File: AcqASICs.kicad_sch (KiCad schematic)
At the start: 54 parts, among them U21 1821-3936, U22 1821-3936

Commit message: Add component values, some more nets
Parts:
- C521, C528, C529, C530, C531, C532, C539, C540, C541, C542, C543, C544: value ? -> 3.3nF
- C523, C524, C525, C526, C527, C534, C535, C536, C537, C538: value ? -> 360pF
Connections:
- net U21_BI18 is gone; now on net U21_BI8: U21.R26 (SIOR)
- net IDB12: now reaches U22.D18 (IDB12)
- net IDB12: now also U21.D18 (IDB12)
- net IDB6: now reaches U22.D19 (IDB6)
- net IDB6: now also U21.D19 (IDB6)
- net IDB0: now reaches U22.D20 (IDB0)
- net IDB0: now also U21.D20 (IDB0)
- net IDB4: now reaches U22.E19 (IDB4)
- net IDB4: now also U21.E19 (IDB4)
- net U39_15: now reaches U22.AA2 (V8.15)
- net U52_9: now reaches U22.AA4 (V5.9)
- net U52_7: now reaches U22.AA5 (V5.7)
- net U52_10: now reaches U22.AB3 (V5.10)
- net U52_4: now reaches U22.AB4 (V5.4)
- net U52_6: now reaches U22.AB5 (V5.6)
- net U52_5: now reaches U22.AC2 (V5.5)
- net U52_13: now reaches U22.AC3 (V5.13)
- net U52_1: now reaches U22.AC4 (V5.1)
- net U52_11: now reaches U22.AC5 (V5.11)
- net U52_12: now reaches U22.AD1 (V5.12)
- net U52_2: now reaches U22.AD2 (V5.2)
- net U52_0: now reaches U22.AD3 (V5.0)
- net U52_3: now reaches U22.AD5 (V5.3)
- net U42_11: now reaches U22.AE10 (V7.11)
- net U42_6: now reaches U22.AE11 (V7.6)
- net U42_8: now reaches U22.AE12 (V7.8)
- net U52_15: now reaches U22.AE2 (V5.15)
- net U52_14: now reaches U22.AE4 (V5.14)
- net U32_14: now reaches U22.AE5 (V6.14)
- net U32_6: now reaches U22.AE6 (V6.6)
- net U32_8: now reaches U22.AE7 (V6.8)
- net U42_14: now reaches U22.AE8 (V7.14)
- net U42_3: now reaches U22.AE9 (V7.3)
- net U42_5: now reaches U22.AF10 (V7.5)
- net U42_9: now reaches U22.AF11 (V7.9)
- net U32_0: now reaches U22.AF2 (V6.0)
- net U32_1: now reaches U22.AF3 (V6.1)
- net U32_12: now reaches U22.AF4 (V6.12)
- net U32_4: now reaches U22.AF5 (V6.4)
- net U32_9: now reaches U22.AF6 (V6.9)
- net U42_0: now reaches U22.AF7 (V7.0)
- net U42_2: now reaches U22.AF8 (V7.2)
- net U42_12: now reaches U22.AF9 (V7.12)
- net U42_10: now reaches U22.AG10 (V7.10)
- net U42_7: now reaches U22.AG11 (V7.7)
- net U32_15: now reaches U22.AG2 (V6.15)
- net U32_2: now reaches U22.AG3 (V6.2)
- net U32_10: now reaches U22.AG4 (V6.10)
- net U32_11: now reaches U22.AG5 (V6.11)
- net U32_7: now reaches U22.AG6 (V6.7)
- net U42_15: now reaches U22.AG7 (V7.15)
- net U42_13: now reaches U22.AG8 (V7.13)
- net U42_4: now reaches U22.AG9 (V7.4)
- net U32_3: now reaches U22.AH2 (V6.3)
- net U32_5: now reaches U22.AH3 (V6.5)
- net U50_4: now reaches U22.B3 (V1.4)
- net U58_11: now reaches U22.C10 (V0.11)
- net U58_6: now reaches U22.C11 (V0.6)
- net U58_8: now reaches U22.C12 (V0.8)
- net U50_11: now reaches U22.C4 (V1.11)
- net U50_12: now reaches U22.C5 (V1.12)
- net U50_6: now reaches U22.C6 (V1.6)
- net U50_8: now reaches U22.C7 (V1.8)
- net U58_14: now reaches U22.C8 (V0.14)
- net U58_3: now reaches U22.C9 (V0.3)
- net U58_4: now reaches U22.D10 (V0.4)
- net U58_10: now reaches U22.D11 (V0.10)
- net U58_7: now reaches U22.D12 (V0.7)
- net U50_15: now reaches U22.D14 (V1.15)
- net U50_0: now reaches U22.D2 (V1.0)
- net U50_1: now reaches U22.D3 (V1.1)
- net U50_3: now reaches U22.D4 (V1.3)
- net U50_13: now reaches U22.D5 (V1.13)
- net U50_10: now reaches U22.D6 (V1.10)
- net U50_7: now reaches U22.D7 (V1.7)
- net U58_1: now reaches U22.D8 (V0.1)
- net U58_13: now reaches U22.D9 (V0.13)
- net U58_12: now reaches U22.E10 (V0.12)
- net U58_5: now reaches U22.E11 (V0.5)
- net U58_9: now reaches U22.E12 (V0.9)
- net U50_2: now reaches U22.E13 (V1.2)
- net U30_15: now reaches U22.E2 (V2.15)
- net U30_1: now reaches U22.E3 (V2.1)
- net U30_0: now reaches U22.E4 (V2.0)
- net U50_14: now reaches U22.E5 (V1.14)
- net U50_5: now reaches U22.E6 (V1.5)
- net U50_9: now reaches U22.E7 (V1.9)
- net U58_15: now reaches U22.E8 (V0.15)
- net U58_2: now reaches U22.E9 (V0.2)
- net U30_11: now reaches U22.F1 (V2.11)
- net U30_13: now reaches U22.F2 (V2.13)
- net U30_3: now reaches U22.F3 (V2.3)
- net U30_2: now reaches U22.F4 (V2.2)
- net U30_14: now reaches U22.F5 (V2.14)
- net U30_10: now reaches U22.G2 (V2.10)
- net U30_5: now reaches U22.G3 (V2.5)
- net U30_4: now reaches U22.G4 (V2.4)
- net U30_12: now reaches U22.G5 (V2.12)
- net U39_0: now reaches U22.H2 (V8.0)
- net U30_7: now reaches U22.H3 (V2.7)
- net U30_6: now reaches U22.H4 (V2.6)
- net U30_9: now reaches U22.H5 (V2.9)
- net U39_1: now reaches U22.J2 (V8.1)
- net U40_15: now reaches U22.J3 (V3.15)
- net U30_8: now reaches U22.J4 (V2.8)
- net U40_0: now reaches U22.J5 (V3.0)
- net U39_2: now reaches U22.K2 (V8.2)
- net U40_2: now reaches U22.K3 (V3.2)
- net U40_1: now reaches U22.K4 (V3.1)
- net U40_14: now reaches U22.K5 (V3.14)
- net U39_3: now reaches U22.L2 (V8.3)
- net U40_12: now reaches U22.L3 (V3.12)
- net U40_13: now reaches U22.L4 (V3.13)
- net U40_3: now reaches U22.L5 (V3.3)
- net U39_4: now reaches U22.M2 (V8.4)
- net U40_5: now reaches U22.M3 (V3.5)
- net U40_4: now reaches U22.M4 (V3.4)
- net U40_11: now reaches U22.M5 (V3.11)
- net U39_6: now reaches U22.N1 (V8.6)
- net U39_5: now reaches U22.N2 (V8.5)
- net U40_9: now reaches U22.N3 (V3.9)
- net U40_6: now reaches U22.N4 (V3.6)
- net U40_10: now reaches U22.N5 (V3.10)
- net U39_7: now reaches U22.P2 (V8.7)
- net U40_8: now reaches U22.P3 (V3.8)
- net U40_7: now reaches U22.P5 (V3.7)
- net U39_8: now reaches U22.R2 (V8.8)
- net U60_8: now reaches U22.R4 (V4.8)
- net U60_7: now reaches U22.R5 (V4.7)
- net U39_9: now reaches U22.T2 (V8.9)
- net U60_9: now reaches U22.T3 (V4.9)
- net U60_10: now reaches U22.T4 (V4.10)
- net U60_6: now reaches U22.T5 (V4.6)
- net U39_11: now reaches U22.U1 (V8.11)
- net U39_10: now reaches U22.U2 (V8.10)
- net U60_5: now reaches U22.U3 (V4.5)
- net U60_4: now reaches U22.U4 (V4.4)
- net U60_11: now reaches U22.U5 (V4.11)
- net U39_12: now reaches U22.V2 (V8.12)
- net U60_12: now reaches U22.V3 (V4.12)
- net U60_13: now reaches U22.V4 (V4.13)
- net U60_3: now reaches U22.V5 (V4.3)
- net U39_13: now reaches U22.W2 (V8.13)
- net U60_2: now reaches U22.W3 (V4.2)
- net U60_1: now reaches U22.W4 (V4.1)
- net U60_14: now reaches U22.W5 (V4.14)
- net U39_14: now reaches U22.Y2 (V8.14)
- net U60_15: now reaches U22.Y3 (V4.15)
- net U52_8: now reaches U22.Y4 (V5.8)
- net U60_0: now reaches U22.Y5 (V4.0)
- net U29_15: now reaches U21.AA2 (V8.15)
- net U48_9: now reaches U21.AA4 (V5.9)
- net U48_7: now reaches U21.AA5 (V5.7)
- net U48_10: now reaches U21.AB3 (V5.10)
- net U48_4: now reaches U21.AB4 (V5.4)
- net U48_6: now reaches U21.AB5 (V5.6)
- net U48_5: now reaches U21.AC2 (V5.5)
- net U48_13: now reaches U21.AC3 (V5.13)
- net U48_1: now reaches U21.AC4 (V5.1)
- net U48_11: now reaches U21.AC5 (V5.11)
- net U48_12: now reaches U21.AD1 (V5.12)
- net U48_2: now reaches U21.AD2 (V5.2)
- net U48_0: now reaches U21.AD3 (V5.0)
- net U48_3: now reaches U21.AD5 (V5.3)
- net U37_11: now reaches U21.AE10 (V7.11)
- net U37_6: now reaches U21.AE11 (V7.6)
- net U37_8: now reaches U21.AE12 (V7.8)
- net U48_15: now reaches U21.AE2 (V5.15)
- net U48_14: now reaches U21.AE4 (V5.14)
- net U27_14: now reaches U21.AE5 (V6.14)
- net U27_6: now reaches U21.AE6 (V6.6)
- net U27_8: now reaches U21.AE7 (V6.8)
- net U37_14: now reaches U21.AE8 (V7.14)
- net U37_3: now reaches U21.AE9 (V7.3)
- net U37_5: now reaches U21.AF10 (V7.5)
- net U37_9: now reaches U21.AF11 (V7.9)
- net U27_0: now reaches U21.AF2 (V6.0)
- net U27_1: now reaches U21.AF3 (V6.1)
- net U27_12: now reaches U21.AF4 (V6.12)
- net U27_4: now reaches U21.AF5 (V6.4)
- net U27_9: now reaches U21.AF6 (V6.9)
- net U37_0: now reaches U21.AF7 (V7.0)
- net U37_2: now reaches U21.AF8 (V7.2)
- net U37_12: now reaches U21.AF9 (V7.12)
- net U37_10: now reaches U21.AG10 (V7.10)
- net U37_7: now reaches U21.AG11 (V7.7)
- net U27_15: now reaches U21.AG2 (V6.15)
- net U27_2: now reaches U21.AG3 (V6.2)
- net U27_10: now reaches U21.AG4 (V6.10)
- net U27_11: now reaches U21.AG5 (V6.11)
- net U27_7: now reaches U21.AG6 (V6.7)
- net U37_15: now reaches U21.AG7 (V7.15)
- net U37_13: now reaches U21.AG8 (V7.13)
- net U37_4: now reaches U21.AG9 (V7.4)
- net U27_3: now reaches U21.AH2 (V6.3)
- net U27_5: now reaches U21.AH3 (V6.5)
- net U46_4: now reaches U21.B3 (V1.4)
- net U54_11: now reaches U21.C10 (V0.11)
- net U54_6: now reaches U21.C11 (V0.6)
- net U54_8: now reaches U21.C12 (V0.8)
- net U46_11: now reaches U21.C4 (V1.11)
- net U46_12: now reaches U21.C5 (V1.12)
- net U46_6: now reaches U21.C6 (V1.6)
- net U46_8: now reaches U21.C7 (V1.8)
- net U54_14: now reaches U21.C8 (V0.14)
- net U54_3: now reaches U21.C9 (V0.3)
- net U54_4: now reaches U21.D10 (V0.4)
- net U54_10: now reaches U21.D11 (V0.10)
- net U54_7: now reaches U21.D12 (V0.7)
- net U46_15: now reaches U21.D14 (V1.15)
- net U46_0: now reaches U21.D2 (V1.0)
- net U46_1: now reaches U21.D3 (V1.1)
- net U46_3: now reaches U21.D4 (V1.3)
- net U46_13: now reaches U21.D5 (V1.13)
- net U46_10: now reaches U21.D6 (V1.10)
- net U46_7: now reaches U21.D7 (V1.7)
- net U54_1: now reaches U21.D8 (V0.1)
- net U54_13: now reaches U21.D9 (V0.13)
- net U54_12: now reaches U21.E10 (V0.12)
- net U54_5: now reaches U21.E11 (V0.5)
- net U54_9: now reaches U21.E12 (V0.9)
- net U46_2: now reaches U21.E13 (V1.2)
- net U25_15: now reaches U21.E2 (V2.15)
- net U25_1: now reaches U21.E3 (V2.1)
- net U25_0: now reaches U21.E4 (V2.0)
- net U46_14: now reaches U21.E5 (V1.14)
- net U46_5: now reaches U21.E6 (V1.5)
- net U46_9: now reaches U21.E7 (V1.9)
- net U54_15: now reaches U21.E8 (V0.15)
- net U54_2: now reaches U21.E9 (V0.2)
- net U25_11: now reaches U21.F1 (V2.11)
- net U25_13: now reaches U21.F2 (V2.13)
- net U25_3: now reaches U21.F3 (V2.3)
- net U25_2: now reaches U21.F4 (V2.2)
- net U25_14: now reaches U21.F5 (V2.14)
- net U25_10: now reaches U21.G2 (V2.10)
- net U25_5: now reaches U21.G3 (V2.5)
- net U25_4: now reaches U21.G4 (V2.4)
- net U25_12: now reaches U21.G5 (V2.12)
- net U29_0: now reaches U21.H2 (V8.0)
- net U25_7: now reaches U21.H3 (V2.7)
- net U25_6: now reaches U21.H4 (V2.6)
- net U25_9: now reaches U21.H5 (V2.9)
- net U29_1: now reaches U21.J2 (V8.1)
- net U35_15: now reaches U21.J3 (V3.15)
- net U25_8: now reaches U21.J4 (V2.8)
- net U35_0: now reaches U21.J5 (V3.0)
- net U29_2: now reaches U21.K2 (V8.2)
- net U35_2: now reaches U21.K3 (V3.2)
- net U35_1: now reaches U21.K4 (V3.1)
- net U35_14: now reaches U21.K5 (V3.14)
- net U29_3: now reaches U21.L2 (V8.3)
- net U35_12: now reaches U21.L3 (V3.12)
- net U35_13: now reaches U21.L4 (V3.13)
- net U35_3: now reaches U21.L5 (V3.3)
- net U29_4: now reaches U21.M2 (V8.4)
- net U35_5: now reaches U21.M3 (V3.5)
- net U35_4: now reaches U21.M4 (V3.4)
- net U35_11: now reaches U21.M5 (V3.11)
- net U29_6: now reaches U21.N1 (V8.6)
- net U29_5: now reaches U21.N2 (V8.5)
- net U35_9: now reaches U21.N3 (V3.9)
- net U35_6: now reaches U21.N4 (V3.6)
- net U35_10: now reaches U21.N5 (V3.10)
- net U29_7: now reaches U21.P2 (V8.7)
- net U35_8: now reaches U21.P3 (V3.8)
- net U35_7: now reaches U21.P5 (V3.7)
- net U29_8: now reaches U21.R2 (V8.8)
- net U56_8: now reaches U21.R4 (V4.8)
- net U56_7: now reaches U21.R5 (V4.7)
- net U29_9: now reaches U21.T2 (V8.9)
- net U56_9: now reaches U21.T3 (V4.9)
- net U56_10: now reaches U21.T4 (V4.10)
- net U56_6: now reaches U21.T5 (V4.6)
- net U29_11: now reaches U21.U1 (V8.11)
- net U29_10: now reaches U21.U2 (V8.10)
- net U56_5: now reaches U21.U3 (V4.5)
- net U56_4: now reaches U21.U4 (V4.4)
- net U56_11: now reaches U21.U5 (V4.11)
- net U29_12: now reaches U21.V2 (V8.12)
- net U56_12: now reaches U21.V3 (V4.12)
- net U56_13: now reaches U21.V4 (V4.13)
- net U56_3: now reaches U21.V5 (V4.3)
- net U29_13: now reaches U21.W2 (V8.13)
- net U56_2: now reaches U21.W3 (V4.2)
- net U56_1: now reaches U21.W4 (V4.1)
- net U56_14: now reaches U21.W5 (V4.14)
- net U29_14: now reaches U21.Y2 (V8.14)
- net U56_15: now reaches U21.Y3 (V4.15)
- net U48_8: now reaches U21.Y4 (V5.8)
- net U56_0: now reaches U21.Y5 (V4.0)
- net ACQ1_CAP1 renamed POD2A_VREF
- net POD2A_VREF: now also U21.Y26 (VREF3); no longer U21.Y26 (CAP4)
- net ACQ1_CAP2 renamed POD1A_VREF
- net POD1A_VREF: now also U21.Y25 (VREF1); no longer U21.Y25 (CAP3)
- net ACQ1_CAP3 renamed POD1B_VREF
- net POD1B_VREF: now also U21.L25 (VREF2); no longer U21.L25 (CAP2)
- net ACQ1_CAP4 renamed POD2B_VREF
- net POD2B_VREF: now also U21.K26 (VREF4); no longer U21.K26 (CAP1)
- net ACQ2_CAP1 renamed POD4A_VREF
- net POD4A_VREF: now also U22.Y26 (VREF3); no longer U22.Y26 (CAP4)
- net ACQ2_CAP2 renamed POD3A_VREF
- net POD3A_VREF: now also U22.Y25 (VREF1); no longer U22.Y25 (CAP3)
- net ACQ2_CAP3 renamed POD3B_VREF
- net POD3B_VREF: now also U22.L25 (VREF2); no longer U22.L25 (CAP2)
- net ACQ2_CAP4 renamed POD4B_VREF
- net POD4B_VREF: now also U22.K26 (VREF4); no longer U22.K26 (CAP1)
- new net IDB1: U21.E20 (IDB1), U22.E20 (IDB1)
- new net IDB10: U21.E18 (IDB10), U22.E18 (IDB10)
- new net IDB11: U21.D22 (IDB11), U22.D22 (IDB11)
- new net IDB13: U21.E22 (IDB13), U22.E22 (IDB13)
- new net IDB14: U21.C18 (IDB14), U22.C18 (IDB14)
- new net IDB15: U21.D23 (IDB15), U22.D23 (IDB15)
- new net IDB2: U21.C20 (IDB2), U22.C20 (IDB2)
- new net IDB3: U21.C21 (IDB3), U22.C21 (IDB3)
- new net IDB5: U21.D21 (IDB5), U22.D21 (IDB5)
- new net IDB7: U21.E21 (IDB7), U22.E21 (IDB7)
- new net IDB8: U21.C19 (IDB8), U22.C19 (IDB8)
- new net IDB9: U21.C22 (IDB9), U22.C22 (IDB9)
- new net U27_13: U21.AE13 (V6.13)
- new net U32_13: U22.AE13 (V6.13)
- new net U37_1: U21.AJ6 (V7.1)
- new net U42_1: U22.AJ6 (V7.1)
- new net U54_0: U21.A6 (V0.0)
- new net U58_0: U22.A6 (V0.0)
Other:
- moved on the sheet: C522, C523, C524, C525, C526, C527, C528, C529, C530, C531, C532, C533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

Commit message: complete outer layers
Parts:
- C522, C533: value 0.47uF -> 4.7uF; footprint Capacitor_Tantalum_SMD:CP_EIA-3528-21_Kemet-B -> hp16717:HP_CP_EIA-3528
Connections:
- net AAA2: now also U22.D16 (AAA); no longer U22.AF16 (AAA)
- net GND: now also U21.D16 (AAA), U22.AF16 (AAA); no longer U21.D16 (GND), U22.D16 (GND)
- net U22_FPGA5: now reaches U22.A13 (FPGA)
- net U22_FPGA4: now reaches U22.A17 (FPGA)
- net U22_FPGA2: now reaches U22.AE20 (FPGA)
- net U22_FPGA3: now reaches U22.AE21 (FPGA)
- net FA_UNK1: now reaches U22.AE22 (FPGA)
- net FA_UNK1: now also U21.AE22 (FPGA)
- net FPGA_ASIC_XC2: now reaches U22.AE23 (FPGA)
- net FPGA_ASIC_XC2: now also U21.AF24 (UNK)
- net U22_FPGA0: now reaches U22.AF20 (FPGA)
- net U22_FPGA1: now reaches U22.AF21 (FPGA)
- net FPGA_ASIC_XC1: now reaches U22.AF24 (UNK)
- net FPGA_ASIC_XC1: now also U21.AE23 (FPGA)
- net U22_SYSCLK_P: now reaches U22.D24 (100MHZ)
- net U22_SYSCLK_N: now reaches U22.D25 (~{100MHZ})
- net IDB_CLK: now reaches U22.E23 (IDB_CLK)
- net IDB_CLK: now also U21.E23 (IDB_CLK)
- net U22_FPGA7: now reaches U22.F25 (FPGA)
- net U22_FPGA6: now reaches U22.G25 (FPGA)
- net U21_FPGA5: now reaches U21.A13 (FPGA)
- net U21_FPGA4: now reaches U21.A17 (FPGA)
- net U21_FPGA2: now reaches U21.AE20 (FPGA)
- net U21_FPGA3: now reaches U21.AE21 (FPGA)
- net U21_FPGA0: now reaches U21.AF20 (FPGA)
- net U21_FPGA1: now reaches U21.AF21 (FPGA)
- net U21_SYSCLK_P: now reaches U21.D24 (100MHZ)
- net U21_SYSCLK_N: now reaches U21.D25 (~{100MHZ})
- net U21_FPGA7: now reaches U21.F25 (FPGA)
- net U21_FPGA6: now reaches U21.G25 (FPGA)
- net VSC17: now reaches U22.AB2 (VSC8)
- net VSC14: now reaches U22.AD4 (VSC4-5B)
- net VSC13: now reaches U22.AE3 (VSC4-5A)
- net VSC16: now reaches U22.AF12 (VSC6-7B)
- net VSC15: now reaches U22.AG12 (VSC6-7A)
- net VSC9: now reaches U22.C2 (VSC0-1A)
- net VSC10: now reaches U22.C3 (VSC0-1B)
- net VSC12: now reaches U22.P4 (VSC2-3B)
- net VSC11: now reaches U22.R3 (VSC2-3A)
- net VSC8: now reaches U21.AB2 (VSC8)
- net VSC5: now reaches U21.AD4 (VSC4-5B)
- net VSC4: now reaches U21.AE3 (VSC4-5A)
- net VSC7: now reaches U21.AF12 (VSC6-7B)
- net VSC6: now reaches U21.AG12 (VSC6-7A)
- net VSC0: now reaches U21.C2 (VSC0-1A)
- net VSC1: now reaches U21.C3 (VSC0-1B)
- net VSC3: now reaches U21.P4 (VSC2-3B)
- net VSC2: now reaches U21.R3 (VSC2-3A)
- net AP1_CLK renamed AP1_CLK_P
- net AP2_CLK renamed AP2_CLK_P
- net AP3_CLK renamed AP3_CLK_P
- net AP4_CLK renamed AP4_CLK_P
- net ~{AP1_CLK} renamed AP1_CLK_N
- net ~{AP2_CLK} renamed AP2_CLK_N
- net ~{AP3_CLK} renamed AP3_CLK_N
- net ~{AP4_CLK} renamed AP4_CLK_N
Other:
- note added: "TODO: Group up BI interface pins"
- note added: "TODO: Move AAA pins to BI interface"
- note added: "to U21 AE23, U22 AF24"
- note added: "to U21 AF24, U22 AE23"

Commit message: schematic cleanup, arrange silk designators
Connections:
- net GND: now also U21.D16 (N_REFL), U22.AF16 (S_REFL); no longer U21.D16 (AAA), U22.AF16 (AAA)
- net U22_VBB_BI: now reaches U22.P25 (NIOR_VREF), U22.T26 (SIOR_VREF)
- net U21_VBB_BI: now reaches U21.P25 (NIOR_VREF), U21.T26 (SIOR_VREF)
- removed net AAA1: RP12.15 (R2.2), RP12.16 (R1.2), U21.AE14 (AAA), U21.AF16 (AAA), U21.E14 (AAA)
- removed net AAA2: RP13.1 (R1.1), RP13.2 (R2.1), U22.AE14 (AAA), U22.D16 (AAA), U22.E14 (AAA)
- new net U21_RBI: RP12.15 (R2.2), RP12.16 (R1.2), U21.AE14 (S_REFH), U21.AF16 (S_REFL), U21.E14 (N_REFH)
- new net U22_RBI: RP13.1 (R1.1), RP13.2 (R2.1), U22.AE14 (S_REFH), U22.D16 (N_REFL), U22.E14 (N_REFH)
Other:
- note added: "2 volts"
- note added: "C13"
- note added: "C17"
- note added: "D13"
- note added: "D15"
- note added: "D17"
- note added: "E15"
- note added: "N26"
- note added: "N27"
- note added: "P26"
- note added: "P27"
- note added: "P28"
- note added: "R25"
- note added: "R26"
- note added: "R27"
- note added: "T27"
- note added: "T28"
- note added: "U26"
- note added: "U27"
- note removed: "TODO: Group up BI interface pins"
- note removed: "TODO: Move AAA pins to BI interface"
- moved on the sheet: C521, C544, R472, R473, R474, R475, R476, R477, R490, R491, R505, R517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

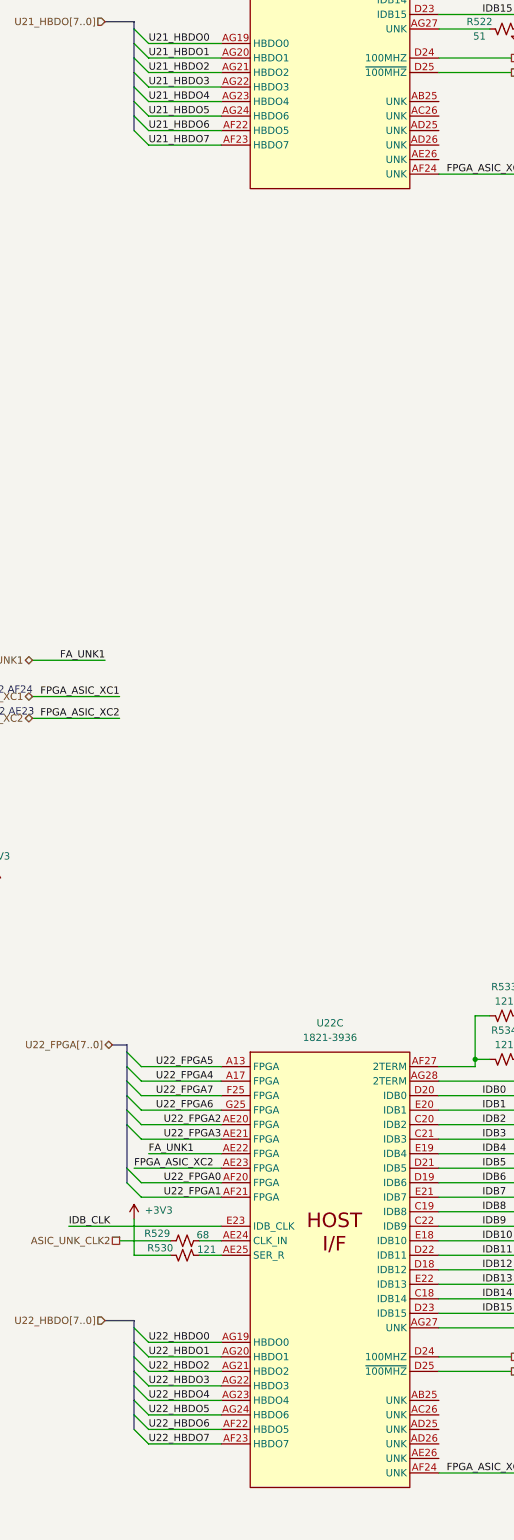
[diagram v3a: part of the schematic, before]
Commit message: numerous small fixes, add plane and inner signal layers
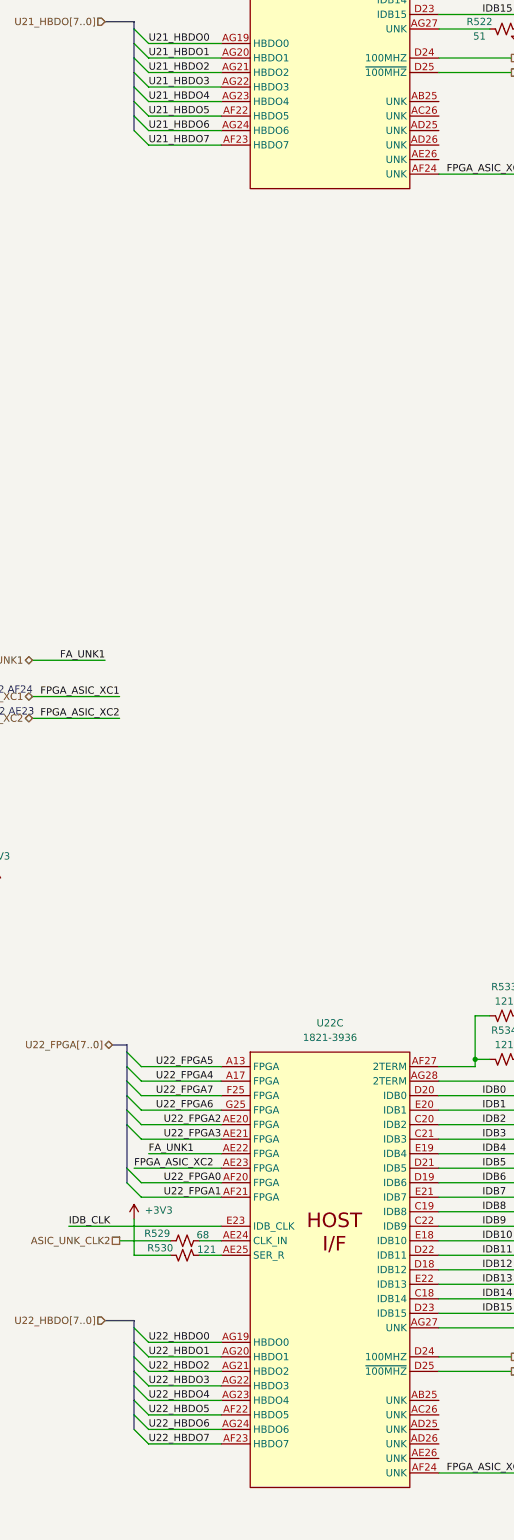
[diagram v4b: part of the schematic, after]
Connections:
- net U21_HBDO5: now also U21.AF22 (HBDO5); no longer U21.AG24 (HBDO6)
- net U21_HBDO6: now also U21.AG24 (HBDO6); no longer U21.AF22 (HBDO5)
- net U22_HBDO5: now also U22.AF22 (HBDO5); no longer U22.AG24 (HBDO6)
- net U22_HBDO6: now also U22.AG24 (HBDO6); no longer U22.AF22 (HBDO5)

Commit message: schematic tweaks, finish innermost layers
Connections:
- net at RP12.10 (R7.2), U21.AG17 (S_BI12): now also RP13.7 (R7.1), U22.C17 (N_BI1)
- net at RP12.11 (R6.2), U21.AE15 (S_BI10): now also RP13.6 (R6.1), U22.E15 (N_BI3)
- net at RP12.12 (R5.2), U21.AF15 (S_BI9): now also RP13.5 (R5.1), U22.D15 (N_BI4)
- net at RP12.13 (R4.2), U21.AG13 (S_BI8): now also RP13.4 (R4.1), U22.C13 (N_BI5)
- net at RP12.14 (R3.2), U21.AF13 (S_BI7): now also RP13.3 (R3.1), U22.D13 (N_BI6)
- net at RP12.9 (R8.2), U21.AF17 (S_BI11): now also RP13.8 (R8.1), U22.D17 (N_BI2)
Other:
- moved on the sheet: C521, C544, R519, R532, RP12, RP13

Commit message: add test points
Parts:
- added TP691: BI11, hp16717:HP_TP30, symbol Connector:TestPoint_Alt
- added TP692: BI12, hp16717:HP_TP30, symbol Connector:TestPoint_Alt
- added TP693: BI10, hp16717:HP_TP30, symbol Connector:TestPoint_Alt
- added TP694: BI9, hp16717:HP_TP30, symbol Connector:TestPoint_Alt
- added TP695: BI8, hp16717:HP_TP30, symbol Connector:TestPoint_Alt
- added TP696: BI7, hp16717:HP_TP30, symbol Connector:TestPoint_Alt
- added TP697, TP698, TP704, TP707, TP771, TP772, TP774, TP775: ?, hp16717:HP_TP30, symbol Connector:TestPoint_Alt
- added TP699, TP700, TP703, TP769, TP770, TP779, TP782: +3V3, hp16717:HP_TP30, symbol Connector:TestPoint_Alt
- added TP702, TP706, TP708, TP709, TP744, TP780, TP781: GND, hp16717:HP_TP30, symbol Connector:TestPoint_Alt
- added TP710: U22_BI2, hp16717:HP_TP30, symbol Connector:TestPoint_Alt
- added TP711: U22_BI4, hp16717:HP_TP30, symbol Connector:TestPoint_Alt
- added TP712: U22_BI5, hp16717:HP_TP30, symbol Connector:TestPoint_Alt
- added TP741: U22_BI1, hp16717:HP_TP30, symbol Connector:TestPoint_Alt
- added TP742: U22_BI3, hp16717:HP_TP30, symbol Connector:TestPoint_Alt
- added TP743: U22_BI6, hp16717:HP_TP30, symbol Connector:TestPoint_Alt
- added TP773: ASIC_CLK1, hp16717:HP_TP30, symbol Connector:TestPoint_Alt
- added TP776: U21_BI9, hp16717:HP_TP30, symbol Connector:TestPoint_Alt
- added TP777: U21_BI2, hp16717:HP_TP30, symbol Connector:TestPoint_Alt
- added TP783: BI2, hp16717:HP_TP30, symbol Connector:TestPoint_Alt
- added TP784: BI1, hp16717:HP_TP30, symbol Connector:TestPoint_Alt
- added TP785: BI3, hp16717:HP_TP30, symbol Connector:TestPoint_Alt
- added TP786: BI4, hp16717:HP_TP30, symbol Connector:TestPoint_Alt
- added TP787: BI5, hp16717:HP_TP30, symbol Connector:TestPoint_Alt
- added TP788: BI6, hp16717:HP_TP30, symbol Connector:TestPoint_Alt
- added TP828: ASIC_CLK2, hp16717:HP_TP30, symbol Connector:TestPoint_Alt
- added TP830: AP1_D0, hp16717:HP_TP30, symbol Connector:TestPoint_Alt
- added TP831: AP1_D1, hp16717:HP_TP30, symbol Connector:TestPoint_Alt
- added TP832: AP1_D2, hp16717:HP_TP30, symbol Connector:TestPoint_Alt
- added TP833: AP1_D3, hp16717:HP_TP30, symbol Connector:TestPoint_Alt
- added TP834: AP1_D4, hp16717:HP_TP30, symbol Connector:TestPoint_Alt
- added TP835: AP1_D5, hp16717:HP_TP30, symbol Connector:TestPoint_Alt
- added TP836: AP1_D6, hp16717:HP_TP30, symbol Connector:TestPoint_Alt
- added TP837: AP1_D7, hp16717:HP_TP30, symbol Connector:TestPoint_Alt
- added TP838: AP1_D8, hp16717:HP_TP30, symbol Connector:TestPoint_Alt
- added TP839: AP1_D9, hp16717:HP_TP30, symbol Connector:TestPoint_Alt
- added TP840: AP1_D10, hp16717:HP_TP30, symbol Connector:TestPoint_Alt
- added TP841: AP1_D11, hp16717:HP_TP30, symbol Connector:TestPoint_Alt
- added TP842: AP1_D12, hp16717:HP_TP30, symbol Connector:TestPoint_Alt
- added TP843: AP1_D13, hp16717:HP_TP30, symbol Connector:TestPoint_Alt
- added TP844: AP1_D14, hp16717:HP_TP30, symbol Connector:TestPoint_Alt
- added TP845: AP1_D15, hp16717:HP_TP30, symbol Connector:TestPoint_Alt
- added TP846: AP2_D0, hp16717:HP_TP30, symbol Connector:TestPoint_Alt
- added TP847: AP2_D1, hp16717:HP_TP30, symbol Connector:TestPoint_Alt
- added TP848: AP2_D2, hp16717:HP_TP30, symbol Connector:TestPoint_Alt
- added TP849: AP2_D3, hp16717:HP_TP30, symbol Connector:TestPoint_Alt
- added TP850: AP2_D4, hp16717:HP_TP30, symbol Connector:TestPoint_Alt
- added TP851: AP2_D5, hp16717:HP_TP30, symbol Connector:TestPoint_Alt
- added TP852: AP2_D6, hp16717:HP_TP30, symbol Connector:TestPoint_Alt
- added TP853: AP2_D7, hp16717:HP_TP30, symbol Connector:TestPoint_Alt
- added TP854: AP2_D8, hp16717:HP_TP30, symbol Connector:TestPoint_Alt
- added TP855: AP2_D9, hp16717:HP_TP30, symbol Connector:TestPoint_Alt
- added TP856: AP2_D10, hp16717:HP_TP30, symbol Connector:TestPoint_Alt
- added TP857: AP2_D11, hp16717:HP_TP30, symbol Connector:TestPoint_Alt
- added TP858: AP2_D12, hp16717:HP_TP30, symbol Connector:TestPoint_Alt
- added TP859: AP2_D13, hp16717:HP_TP30, symbol Connector:TestPoint_Alt
- added TP860: AP2_D14, hp16717:HP_TP30, symbol Connector:TestPoint_Alt
- added TP861: AP2_D15, hp16717:HP_TP30, symbol Connector:TestPoint_Alt
- added TP862: AP1_CLK_P, hp16717:HP_TP30, symbol Connector:TestPoint_Alt
- added TP863: AP1_CLK_N, hp16717:HP_TP30, symbol Connector:TestPoint_Alt
- added TP864: AP2_CLK_P, hp16717:HP_TP30, symbol Connector:TestPoint_Alt
- added TP865: AP2_CLK_N, hp16717:HP_TP30, symbol Connector:TestPoint_Alt
- added TP866, TP884: AP3_CLK_P, hp16717:HP_TP30, symbol Connector:TestPoint_Alt
- added TP867, TP885: AP3_CLK_N, hp16717:HP_TP30, symbol Connector:TestPoint_Alt
- added TP868, TP886: AP3_D0, hp16717:HP_TP30, symbol Connector:TestPoint_Alt
- added TP869, TP887: AP3_D1, hp16717:HP_TP30, symbol Connector:TestPoint_Alt
- added TP870, TP888: AP3_D2, hp16717:HP_TP30, symbol Connector:TestPoint_Alt
- added TP871, TP889: AP3_D3, hp16717:HP_TP30, symbol Connector:TestPoint_Alt
- added TP872, TP890: AP3_D4, hp16717:HP_TP30, symbol Connector:TestPoint_Alt
- added TP873, TP891: AP3_D5, hp16717:HP_TP30, symbol Connector:TestPoint_Alt
- added TP874, TP892: AP3_D6, hp16717:HP_TP30, symbol Connector:TestPoint_Alt
- added TP875, TP893: AP3_D7, hp16717:HP_TP30, symbol Connector:TestPoint_Alt
- added TP876, TP894: AP3_D8, hp16717:HP_TP30, symbol Connector:TestPoint_Alt
- added TP877, TP895: AP3_D9, hp16717:HP_TP30, symbol Connector:TestPoint_Alt
- added TP878, TP896: AP3_D10, hp16717:HP_TP30, symbol Connector:TestPoint_Alt
- added TP879, TP897: AP3_D11, hp16717:HP_TP30, symbol Connector:TestPoint_Alt
- added TP880, TP898: AP3_D12, hp16717:HP_TP30, symbol Connector:TestPoint_Alt
- added TP881, TP899: AP3_D13, hp16717:HP_TP30, symbol Connector:TestPoint_Alt
- added TP882, TP900: AP3_D14, hp16717:HP_TP30, symbol Connector:TestPoint_Alt
- added TP883, TP901: AP3_D15, hp16717:HP_TP30, symbol Connector:TestPoint_Alt
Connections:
- net +3V3: now also TP699.1, TP700.1, TP703.1, TP769.1, TP770.1, TP779.1, TP782.1
- net AP1_CLK_N: now also TP863.1
- net AP1_CLK_P: now also TP862.1
- net AP1_D0: now also TP830.1
- net AP1_D1: now also TP831.1
- net AP1_D10: now also TP840.1
- net AP1_D11: now also TP841.1
- net AP1_D12: now also TP842.1
- net AP1_D13: now also TP843.1
- net AP1_D14: now also TP844.1
- net AP1_D15: now also TP845.1
- net AP1_D2: now also TP832.1
- net AP1_D3: now also TP833.1
- net AP1_D4: now also TP834.1
- net AP1_D5: now also TP835.1
- net AP1_D6: now also TP836.1
- net AP1_D7: now also TP837.1
- net AP1_D8: now also TP838.1
- net AP1_D9: now also TP839.1
- net AP2_CLK_N: now also TP865.1
- net AP2_CLK_P: now also TP864.1
- net AP2_D0: now also TP846.1
- net AP2_D1: now also TP847.1
- net AP2_D10: now also TP856.1
- net AP2_D11: now also TP857.1
- net AP2_D12: now also TP858.1
- net AP2_D13: now also TP859.1
- net AP2_D14: now also TP860.1
- net AP2_D15: now also TP861.1
- net AP2_D2: now also TP848.1
- net AP2_D3: now also TP849.1
- net AP2_D4: now also TP850.1
- net AP2_D5: now also TP851.1
- net AP2_D6: now also TP852.1
- net AP2_D7: now also TP853.1
- net AP2_D8: now also TP854.1
- net AP2_D9: now also TP855.1
- net AP3_CLK_N: now also TP867.1
- net AP3_CLK_P: now also TP866.1
- net AP3_D0: now also TP868.1
- net AP3_D1: now also TP869.1
- net AP3_D10: now also TP878.1
- net AP3_D11: now also TP879.1
- net AP3_D12: now also TP880.1
- net AP3_D13: now also TP881.1
- net AP3_D14: now also TP882.1
- net AP3_D15: now also TP883.1
- net AP3_D2: now also TP870.1
- net AP3_D3: now also TP871.1
- net AP3_D4: now also TP872.1
- net AP3_D5: now also TP873.1
- net AP3_D6: now also TP874.1
- net AP3_D7: now also TP875.1
- net AP3_D8: now also TP876.1
- net AP3_D9: now also TP877.1
- net AP4_CLK_N: now also TP885.1
- net AP4_CLK_P: now also TP884.1
- net AP4_D0: now also TP893.1
- net AP4_D1: now also TP892.1
- net AP4_D10: now also TP896.1
- net AP4_D11: now also TP897.1
- net AP4_D12: now also TP898.1
- net AP4_D13: now also TP899.1
- net AP4_D14: now also TP900.1
- net AP4_D15: now also TP901.1
- net AP4_D2: now also TP891.1
- net AP4_D3: now also TP890.1
- net AP4_D4: now also TP889.1
- net AP4_D5: now also TP888.1
- net AP4_D6: now also TP887.1
- net AP4_D7: now also TP886.1
- net AP4_D8: now also TP894.1
- net AP4_D9: now also TP895.1
- net ASIC_UNK_CLK1: now also TP773.1
- net ASIC_UNK_CLK2: now also TP828.1
- net BI1: now also TP784.1
- net BI10: now also TP693.1
- net BI11: now also TP691.1
- net BI12: now also TP692.1
- net BI2: now also TP783.1
- net BI3: now also TP785.1
- net BI4: now also TP786.1
- net BI5: now also TP787.1
- net BI6: now also TP788.1
- net BI7: now also TP696.1
- net BI8: now also TP695.1
- net BI9: now also TP694.1
- net GND: now also TP702.1, TP706.1, TP708.1, TP709.1, TP744.1, TP780.1, TP781.1
- net U21_BI2: now also TP777.1
- net U21_BI9: now also TP776.1
- net U22_BI1: now also TP741.1
- net U22_BI2: now also TP710.1
- net U22_BI3: now also TP742.1
- net U22_BI4: now also TP711.1
- net U22_BI5: now also TP712.1
- net U22_BI6: now also TP743.1
- net at R533.1, R534.1, U22.AG28 (2TERM): now also TP698.1
- net at R533.2, R534.2, U22.AF27 (2TERM): now also TP697.1
- net at R519.1, RP12.1 (R1.1): now also TP775.1
- net at R531.2, U22.AG27 (UNK): now also TP704.1
- net at R523.1, R527.1, U21.AG28 (2TERM): now also TP772.1
- net at R523.2, R527.2, U21.AF27 (2TERM): now also TP771.1
- net at R532.1, RP13.16 (R1.2): now also TP707.1
- net at R522.2, U21.AG27 (UNK): now also TP774.1
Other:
- moved on the sheet: C529, C530, C531, C532, C533, C534, C535, C536, C537, C538, C539, R528

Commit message: tweaks and some schematic notes
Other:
- note added: "1.4V"
- note added: "1V"
- note added: "2.03V"
- note added: "2.23V"
- note added: "500mV"
- note added: "Both at 3.36V"
- note removed: "2 volts"
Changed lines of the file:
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@@
+		)
+	)
+	(text "1V"
+		(exclude_from_sim no)
+		(at 478.536 302.26 0)
+		(effects
+			(font
+				(size 1.27 1.27)
+			)
 		)
 	)
@@
 		)
 	)
+	(text "500mV"
+		(exclude_from_sim no)
+		(at 573.532 110.49 0)
+		(effects
+			(font
+				(size 1.27 1.27)
+			)
+		)
+	)
+	(text "2.03V"
+		(exclude_from_sim no)
+		(at 489.204 330.2 0)
+		(effects
+			(font
+				(size 1.27 1.27)
+			)
+		)
+	)
 	(text "R25"
 		(exclude_from_sim no)
@@
 		)
 	)
-	(text "2 volts"
+	(text "2.03V"
 		(exclude_from_sim no)
 		(at 498.856 149.352 0)
@@
 		)
 	)
+	(text "Both at 3.36V"
+		(exclude_from_sim no)
+		(at 262.382 252.984 0)
+		(effects
+			(font
+				(size 1.27 1.27)
+			)
+		)
+	)
 	(text "U27"
 		(exclude_from_sim no)
@@
 		)
 	)
+	(text "1.4V"
+		(exclude_from_sim no)
+		(at 184.404 308.864 0)
+		(effects
+			(font
+				(size 1.27 1.27)
+			)
+		)
+	)
 	(text "P27"
 		(exclude_from_sim no)
@@
 		)
 	)
-	(text "2 volts"
-		(exclude_from_sim no)
-		(at 513.334 329.946 0)
-		(effects
-			(font
-				(size 1.27 1.27)
-			)
-		)
-	)
 	(text "to U21 AE23, U22 AF24"
 		(exclude_from_sim no)
@@
 		)
 	)
+	(text "1V"
+		(exclude_from_sim no)
+		(at 547.624 122.682 0)
+		(effects
+			(font
+				(size 1.27 1.27)
+			)
+		)
+	)
 	(text "P27"
 		(exclude_from_sim no)
@@
 		)
 	)
+	(text "500mV"
+		(exclude_from_sim no)
+		(at 451.104 293.878 0)
+		(effects
+			(font
+				(size 1.27 1.27)
+			)
+		)
+	)
 	(text "T27"
 		(exclude_from_sim no)
@@
 		(effects
 			(font
+				(size 1.27 1.27)
+			)
+		)
+	)
+	(text "2.23V"
+		(exclude_from_sim no)
+		(at 30.734 88.9 0)
+		(effects
+			(font
